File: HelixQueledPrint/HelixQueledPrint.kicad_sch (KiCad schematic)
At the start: 0 parts

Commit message: (S)Created led drivers, started MCU design
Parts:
- added AE101: Antenna_Chip, symbol Device:Antenna_Chip
- added R101, R102: 0R, symbol Device:R
- added U101: ESP32-C6FHx, Package_DFN_QFN:QFN-32-1EP_5x5mm_P0.5mm_EP3.65x3.65mm_ThermalVias, symbol customFootprints:ESP32-C6FHx
- added U102: BGS12WN6E6327, Package_LGA:Infineon_PG-TSNP-6-10_0.7x1.1mm_0.7x1.1mm_P0.4mm, symbol RF_Switch:BGS12WN6E6327
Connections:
- new net: AE101.2 (PCB_Trace), U102.1 (RF2)
- new net: U101.1 (ANT), U102.5 (RFIN)
- new net: R101.1, R102.2, U102.6 (CTRL)
- new net +3V3: R102.1, U102.4 (VDD)
- new net GND: R101.2, U102.2 (GND)
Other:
- added sheet LedDriverBlue (Driver.kicad_sch)
- added sheet LedDriverGreen (Driver.kicad_sch)
- added sheet LedDriverRed (Driver.kicad_sch)
- added sheet LedDriverWhite (Driver.kicad_sch)

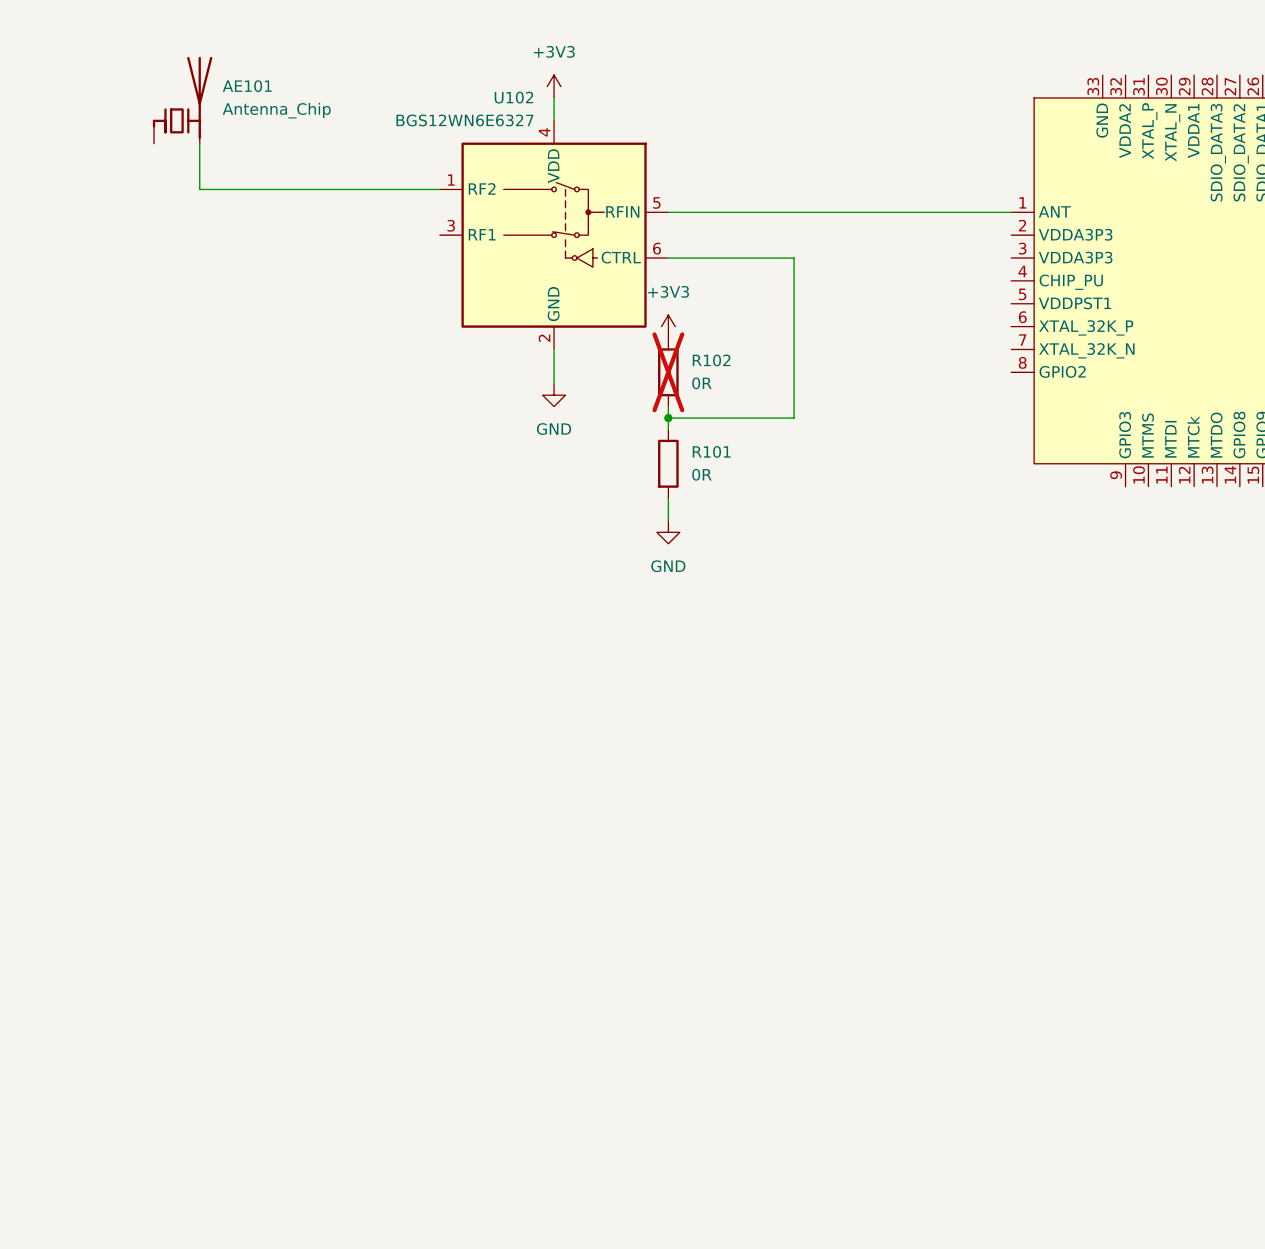
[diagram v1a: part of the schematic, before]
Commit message: 5V Voeding toegevoegd
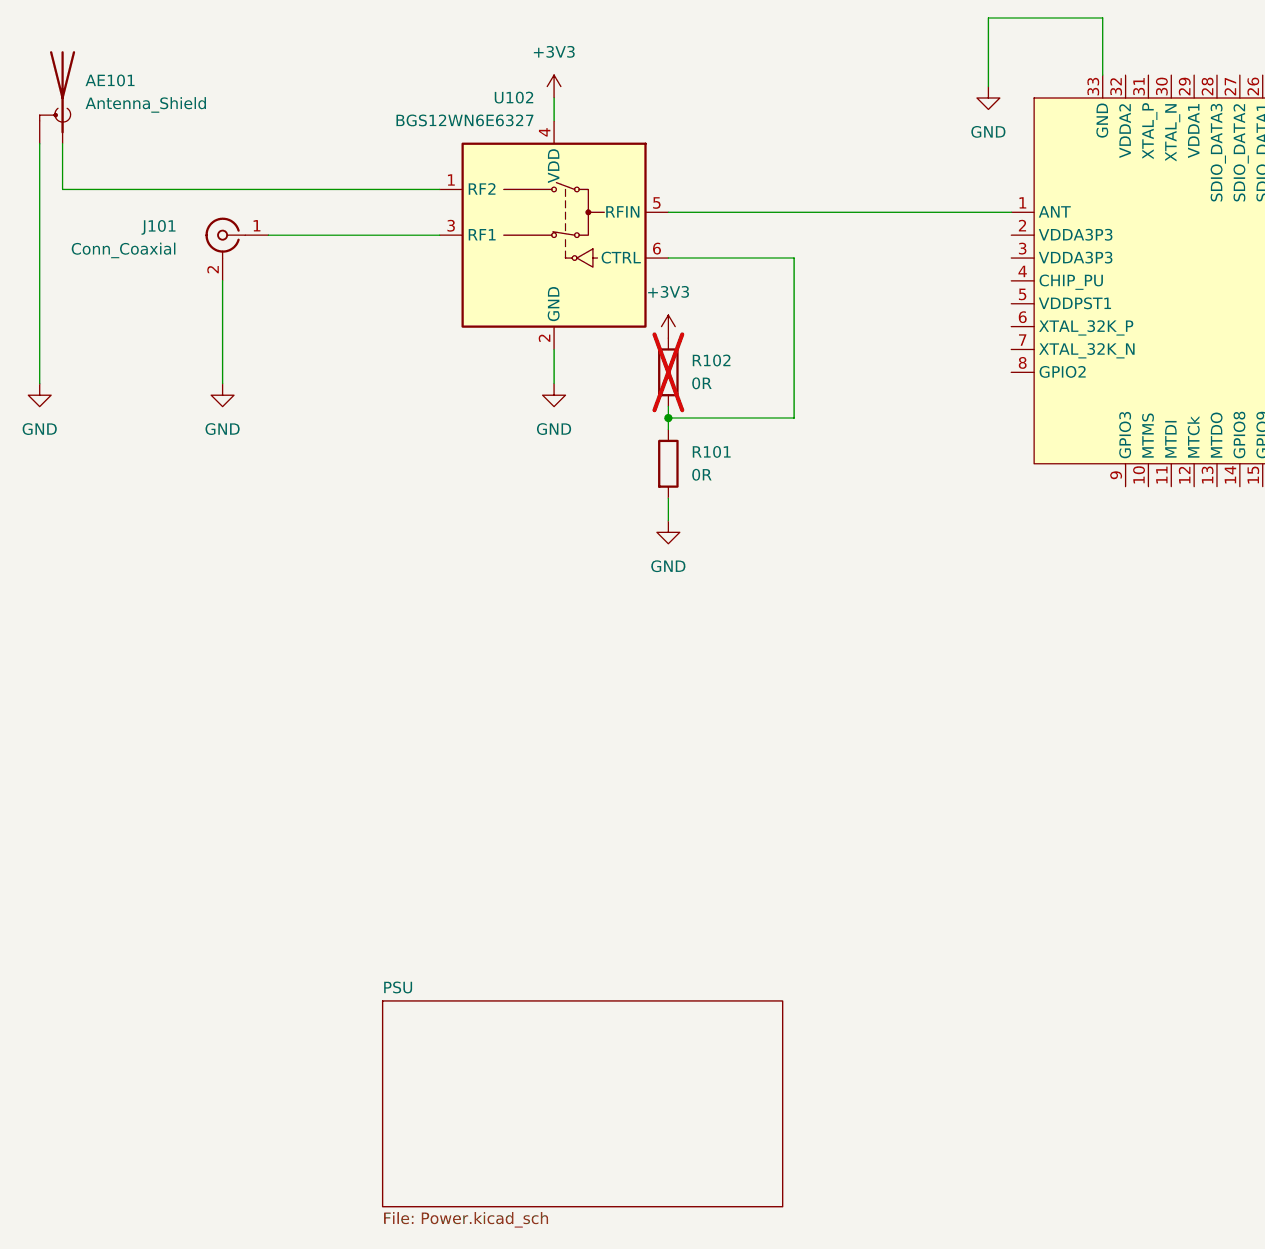
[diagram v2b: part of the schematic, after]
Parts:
- removed AE101: Antenna_Chip, symbol Device:Antenna_Chip
- added AE101: Antenna_Shield, symbol Device:Antenna_Shield
- added J101: Conn_Coaxial, symbol Connector:Conn_Coaxial
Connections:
- net GND: now also U101.33 (GND), AE101.2 (Shield), J101.2 (Ext)
- net at U102.1 (RF2): now also AE101.1 (A)
- net at U102.3 (RF1): now also J101.1 (In)
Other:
- added sheet PSU (Power.kicad_sch)

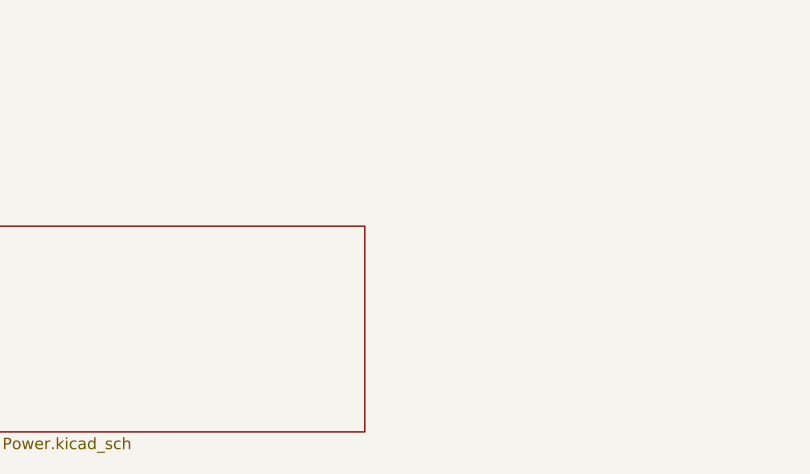
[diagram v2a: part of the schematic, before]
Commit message: 3.3V voeding toegevoegd
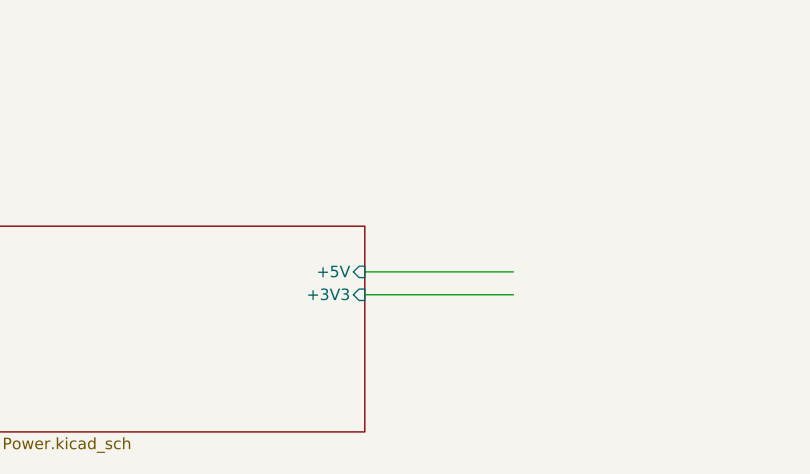
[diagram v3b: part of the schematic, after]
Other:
- sheet PSU ports: added +3V3, +5V; removed none
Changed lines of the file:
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@@
+	(wire
+		(pts
+			(xy 105.41 143.51) (xy 121.92 143.51)
+		)
+		(stroke
+			(width 0)
+			(type default)
+		)
+	)
 	(wire
 		(pts
@@
 		(pts
 			(xy 140.97 29.21) (xy 128.27 29.21)
+		)
+		(stroke
+			(width 0)
+			(type default)
+		)
+	)
+	(wire
+		(pts
+			(xy 105.41 146.05) (xy 121.92 146.05)
 		)
 		(stroke
@@
 			)
 		)
+		(pin "+3V3" input
+			(at 105.41 146.05 0)
+			(effects
+				(font
+					(size 1.27 1.27)
+				)
+				(justify right)
+			)
+		)
+		(pin "+5V" input
+			(at 105.41 143.51 0)
+			(effects
+				(font
+					(size 1.27 1.27)
+				)
+				(justify right)
+			)
+		)

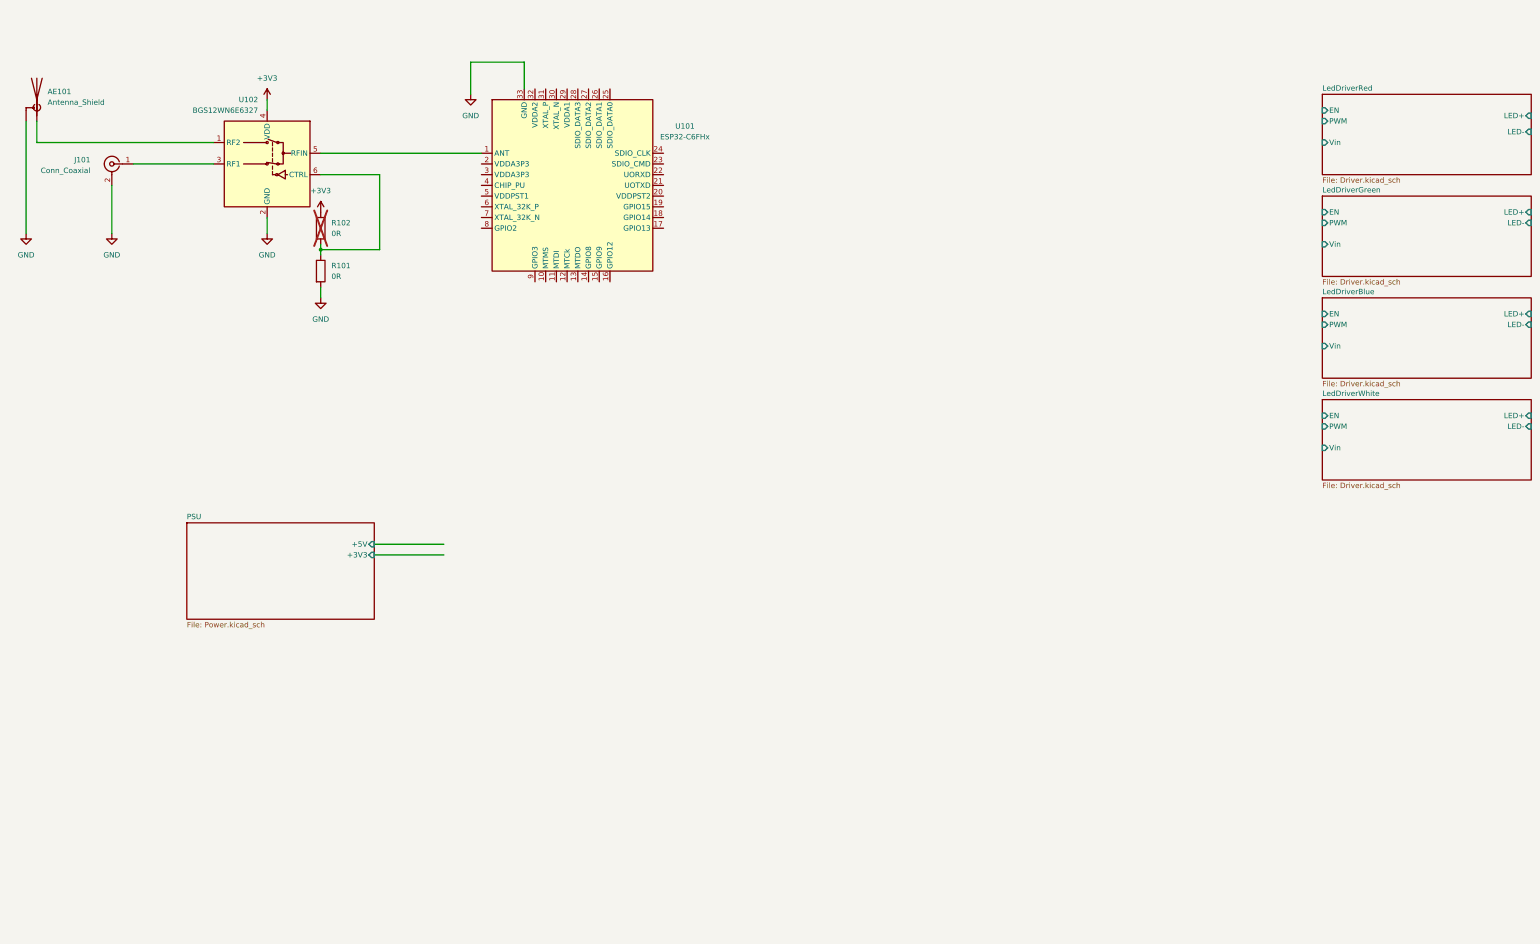
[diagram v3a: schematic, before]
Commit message: USB-c en boot/reset knoppen toegevoegd
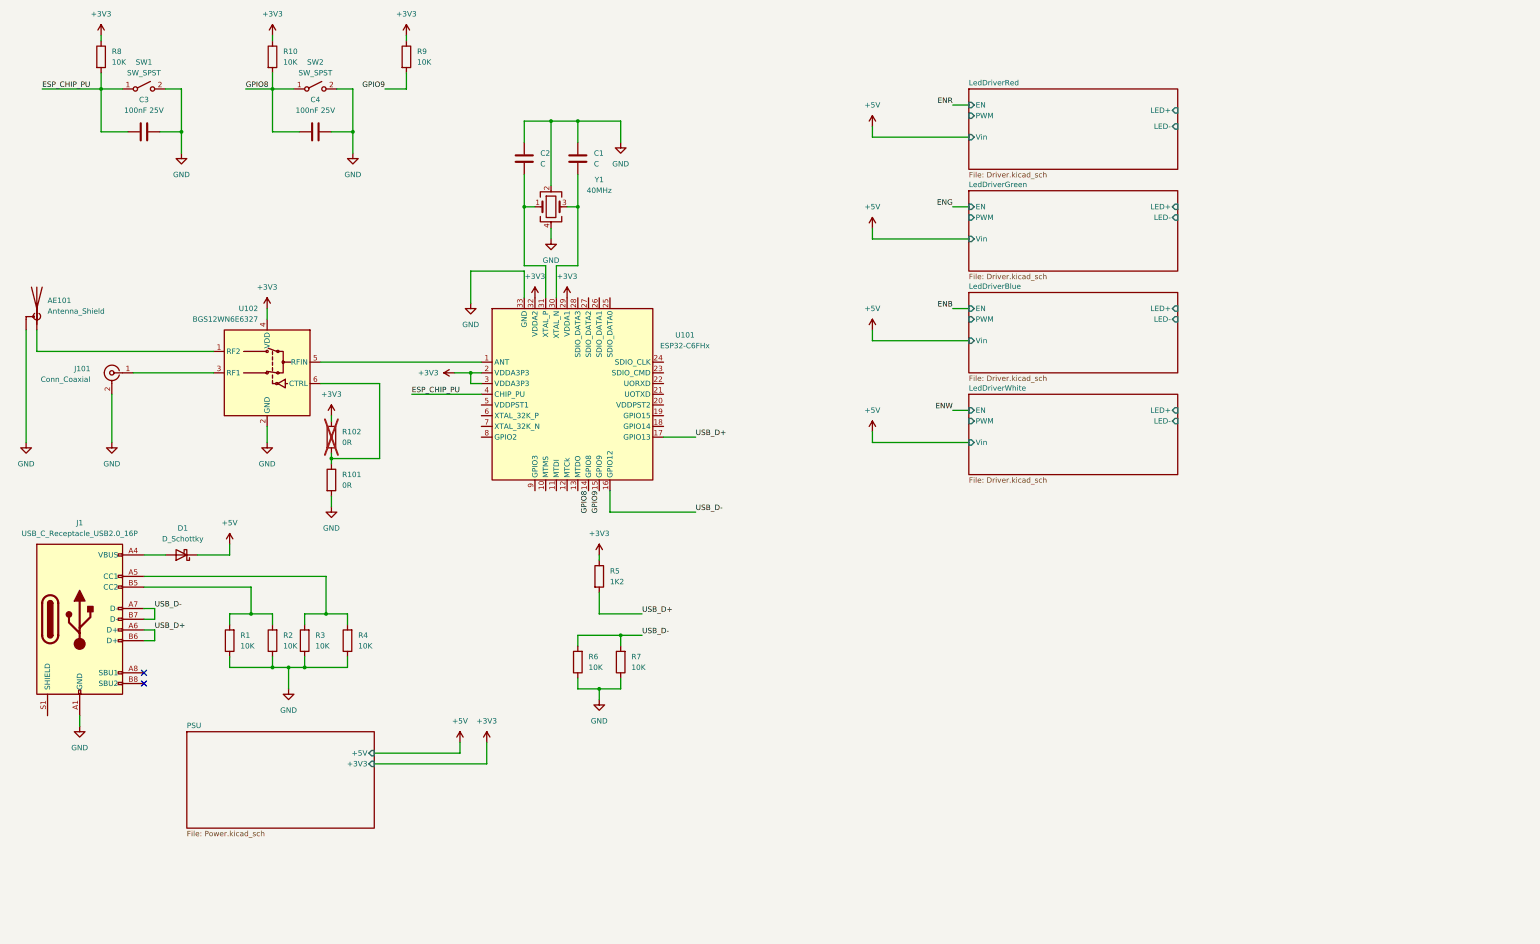
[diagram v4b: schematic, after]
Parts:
- added C1, C2: C, symbol Device:C
- added C3, C4: 100nF 25V, Capacitor_SMD:C_0402_1005Metric, symbol Device:C
- added D1: D_Schottky, symbol Device:D_Schottky
- added J1: USB_C_Receptacle_USB2.0_16P, symbol Connector:USB_C_Receptacle_USB2.0_16P
- added R1, R10, R2, R3, R4, R6, R7, R8, R9: 10K, symbol Device:R
- added R5: 1K2, symbol Device:R
- added SW1, SW2: SW_SPST, symbol Switch:SW_SPST
- added Y1: 40MHz, symbol Device:Crystal_GND24
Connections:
- net +3V3: now also U101.2 (VDDA3P3), U101.29 (VDDA1), U101.3 (VDDA3P3), U101.32 (VDDA2), R10.1, R5.1, R8.1, R9.1
- net GND: now also C1.1, C2.1, C3.1, C4.1, J1.A1 (GND), J1.A12 (GND), J1.B1 (GND), J1.B12 (GND), R1.1, R2.1, R3.1, R4.1, R6.1, R7.1, SW1.2 (B), SW2.2 (B), Y1.2, Y1.4
- net GPIO8: now reaches U101.14 (GPIO8)
- net GPIO8: now also C4.2, R10.2, SW2.1 (A)
- net GPIO9: now reaches U101.15 (GPIO9)
- net GPIO9: now also R9.2
- net USB_D-: now reaches U101.16 (GPIO12)
- net USB_D-: now also J1.A7 (D-), J1.B7 (D-), R6.2, R7.2
- net USB_D+: now reaches U101.17 (GPIO13)
- net USB_D+: now also J1.A6 (D+), J1.B6 (D+), R5.2
- net at U101.30 (XTAL_N): now also C1.2, Y1.3
- net at U101.31 (XTAL_P): now also C2.2, Y1.1
- net ESP_CHIP_PU: now reaches U101.4 (CHIP_PU)
- net ESP_CHIP_PU: now also C3.2, R8.2, SW1.1 (A)
- new net: J1.B5 (CC2), R1.2, R2.2
- new net: J1.A5 (CC1), R3.2, R4.2
- new net: D1.2 (A), J1.A4 (VBUS), J1.A9 (VBUS), J1.B4 (VBUS), J1.B9 (VBUS)
- new net +5V: D1.1 (K)
- no-connect marks 0 -> 2
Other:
- moved on the sheet: AE101, J101, R101, R102, U101, U102

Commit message: GPIO verbindingen gemaakt, en condensatoren toegevoegd
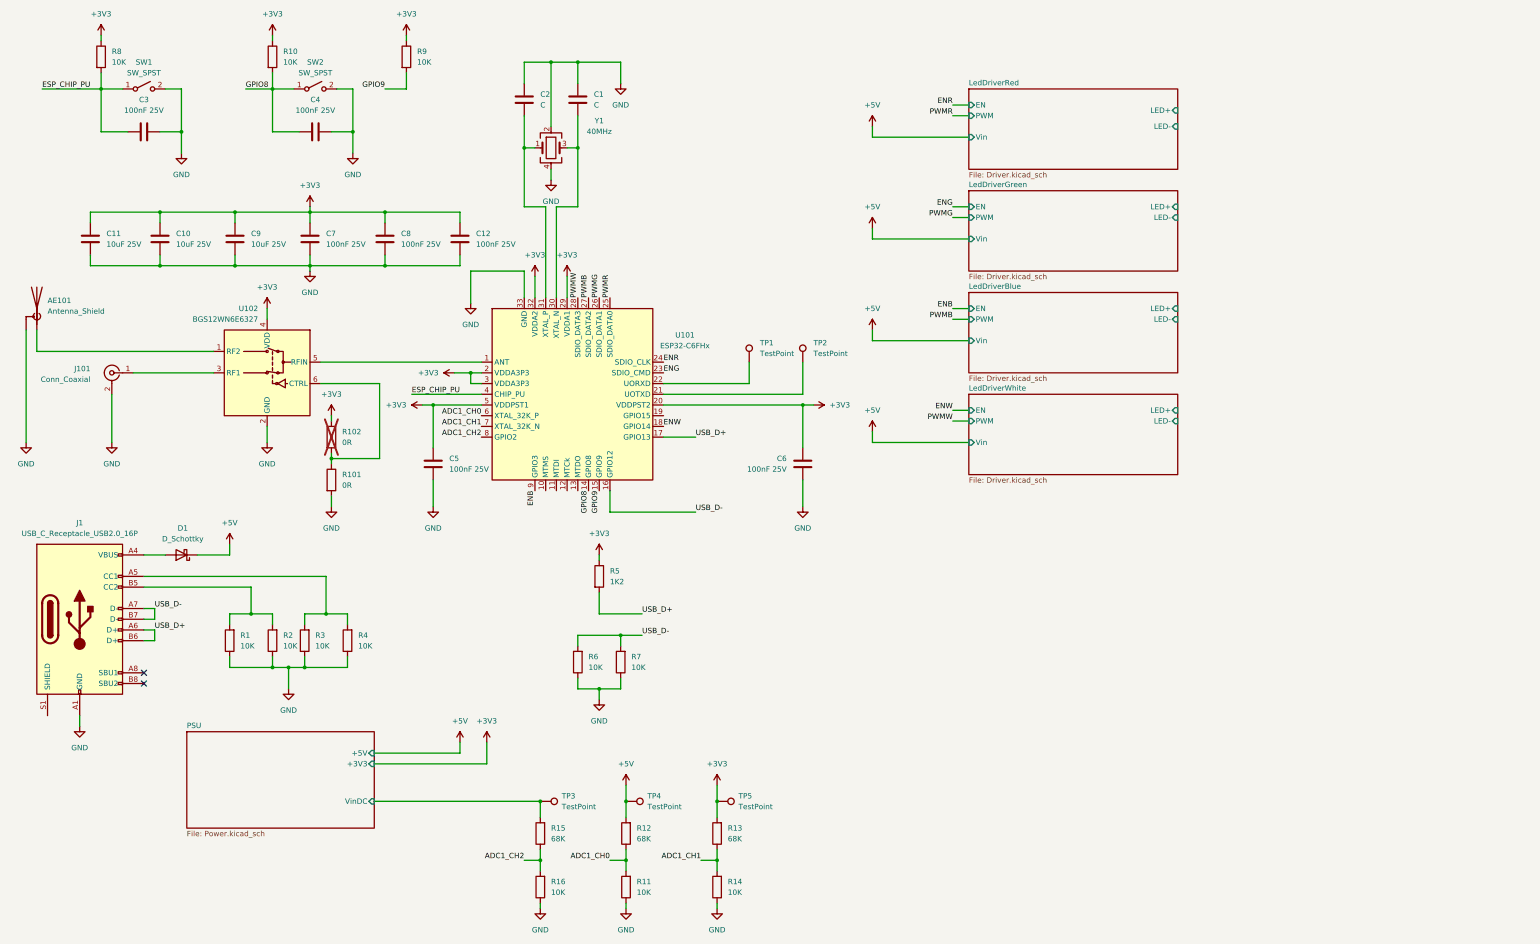
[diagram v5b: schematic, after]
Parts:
- added C10, C11, C9: 10uF 25V, Capacitor_SMD:C_0805_2012Metric, symbol Device:C
- added C12, C5, C6, C7, C8: 100nF 25V, Capacitor_SMD:C_0402_1005Metric, symbol Device:C
- added R11, R14, R16: 10K, symbol Device:R
- added R12, R13, R15: 68K, symbol Device:R
- added TP1, TP2, TP3, TP4, TP5: TestPoint, symbol Connector:TestPoint
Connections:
- net +3V3: now also U101.20 (VDDPST2), U101.5 (VDDPST1), C10.1, C11.1, C12.1, C5.1, C6.1, C7.1, C8.1, C9.1, R13.2, TP5.1
- net +5V: now also R12.2, TP4.1
- net ENB: now also U101.9 (GPIO3)
- net ENG: now also U101.23 (SDIO_CMD)
- net ENR: now also U101.24 (SDIO_CLK)
- net ENW: now also U101.18 (GPIO14)
- net GND: now also C10.2, C11.2, C12.2, C5.2, C6.2, C7.2, C8.2, C9.2, R11.1, R14.1, R16.1
- net at U101.21 (UOTXD): now also TP2.1
- net at U101.22 (UORXD): now also TP1.1
- net PWMR: now reaches U101.25 (SDIO_DATA0)
- net PWMG: now reaches U101.26 (SDIO_DATA1)
- net PWMB: now reaches U101.27 (SDIO_DATA2)
- net PWMW: now reaches U101.28 (SDIO_DATA3)
- net ADC1_CH0: now reaches U101.6 (XTAL_32K_P)
- net ADC1_CH0: now also R11.2, R12.1
- net ADC1_CH1: now reaches U101.7 (XTAL_32K_N)
- net ADC1_CH1: now also R13.1, R14.2
- net ADC1_CH2: now reaches U101.8 (GPIO2)
- net ADC1_CH2: now also R15.1, R16.2
- new net PSU/VinDC: R15.2, TP3.1
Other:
- sheet PSU ports: added VinDC; removed none
- moved on the sheet: C1, C2, Y1
